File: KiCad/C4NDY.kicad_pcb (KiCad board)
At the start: 2 copper layers, 22.9 x 50.2 mm, 43 parts, among them J1 Conn_01x08, J2 Conn_01x07, J3 Conn_01x05, J4 5077CR-16SMC2-BK-TR, J5 Conn_01x06, J6 Conn_01x08, J7 FTSH-105-01-L-DV-K, SW1 SKRPABE010, SW2 SKRPABE010, U1 MIC39100-3.3WS, U2 IS66WVS2M8BLL, U3 STM32G4A1CETx, X1 SG-310SCF

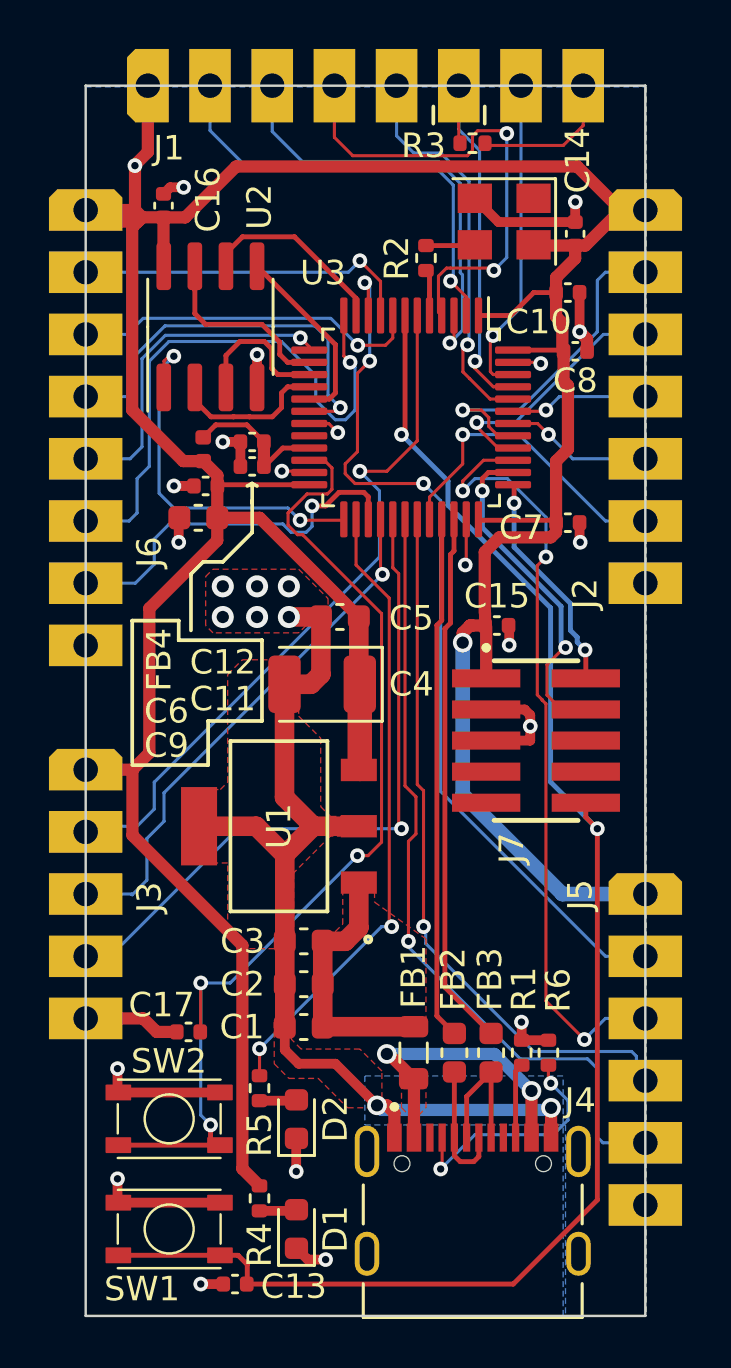
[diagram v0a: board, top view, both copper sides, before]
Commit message: VrefをVCCに接続し、マイコン周辺の部品配置と配線を修正
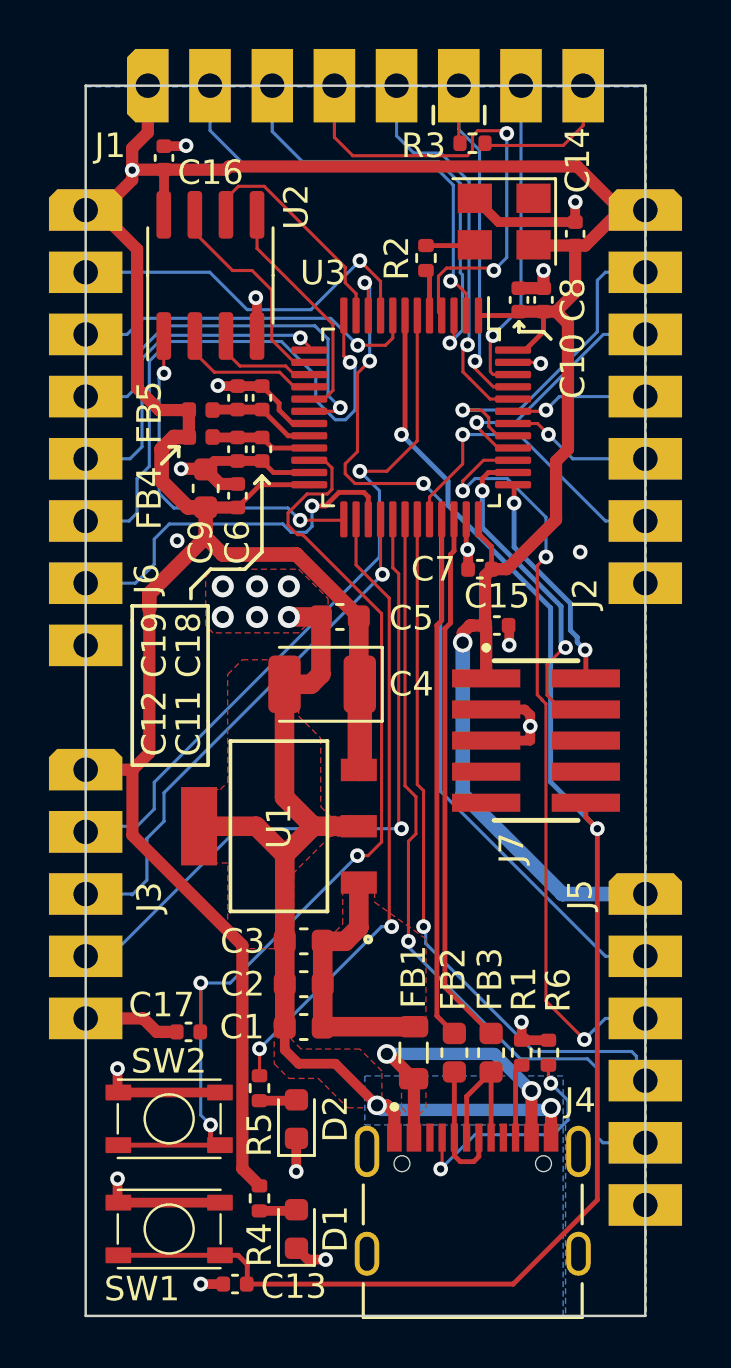
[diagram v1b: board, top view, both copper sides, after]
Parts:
- added C18: 100nF, Capacitor_SMD:C_0402_1005Metric, F.Cu at (137.2, 92.5)
- added C19: 1uF, Capacitor_SMD:C_0402_1005Metric, F.Cu at (136.2, 92.5)
- added FB5: BLM15PX601SN1D, Inductor_SMD:L_0402_1005Metric, F.Cu at (134.7, 93.0)
- moved C7 4.07 mm to (146.1, 99.5), turned to 180 degrees
- moved C8 2.47 mm to (148.7, 88.5), turned to 90 degrees
- moved U2 2.10 mm to (135.1, 87.5)
- moved C10 2.02 mm to (147.7, 88.5), turned to 90 degrees
- moved C16 1.95 mm to (133.2, 82.7)
- moved C6 1.36 mm to (136.2, 96.5), turned to 90 degrees
- moved C9 1.24 mm to (134.9, 96.2), turned to 90 degrees
- moved C11 0.81 mm to (137.2, 94.6), turned to -90 degrees
- moved C12 0.67 mm to (136.2, 94.6), turned to -90 degrees
- moved FB4 0.51 mm to (134.7, 94.1), turned to 180 degrees
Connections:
- U3 pad 20: unconnected-(U3-VREF+-Pad20) -> Net-(U3-VREF+)
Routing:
- net Net-(U3-VREF+): track 0.00 -> 4.40 mm
- net GND: track 93.5 -> 97.7 mm, vias 28 -> 26
- net /QSPI_IO2: track 6.62 -> 4.44 mm
- net Net-(U3-VDDA): track 6.14 -> 4.13 mm
- net /ADC1_IN2: track 13.0 -> 14.9 mm
- net /QSPI_IO0: track 7.67 -> 9.57 mm
- net /QSPI_IO1: track 6.89 -> 5.93 mm
- net /QSPI_NCS: track 15.4 -> 14.5 mm
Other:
- board text added: "rev.C"
- board text removed: "rev.B"
